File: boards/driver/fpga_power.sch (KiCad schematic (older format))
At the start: 30 parts, among them J1 Barrel_Jack, Q90 IRF530, U10 74LVC245, U11 JTE0624D05, U12 LTC4231-1, U13 74HC4514, U14 74LVC2G04, U15 74LVC2G04, U16 74LVC2G04, U17 74LVC2G04, U9 74LVC245

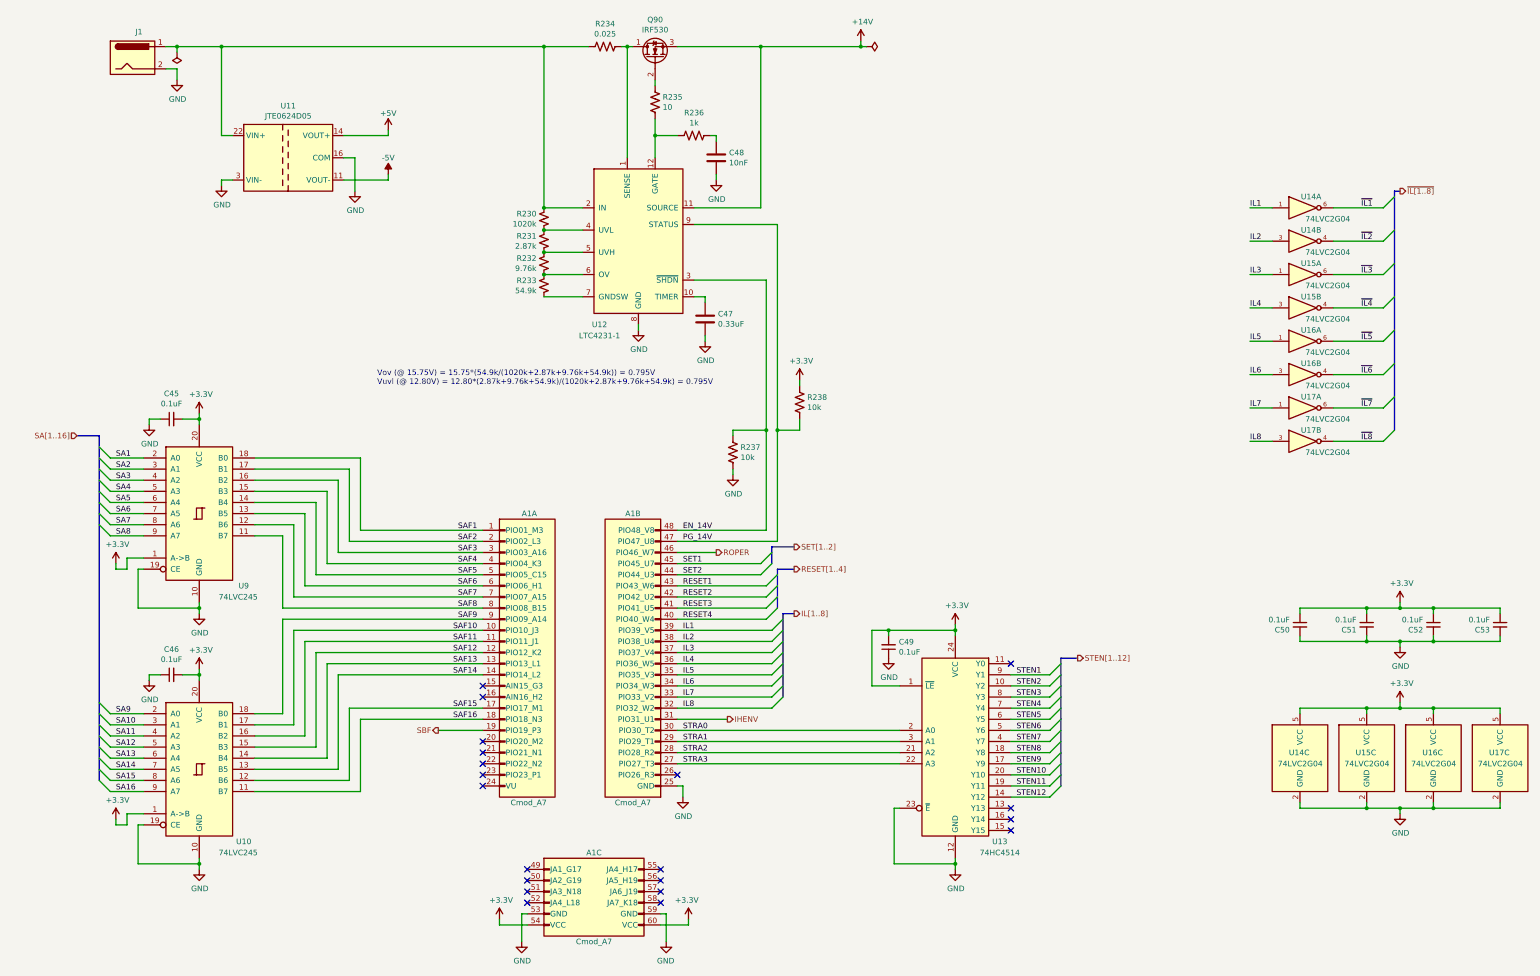
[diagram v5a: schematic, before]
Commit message: Driver board: significant cleanup. Moved sense amp pairs into a subsheet, split tuning resistors into two globally, pushed input circuits into their corresponding sheets.
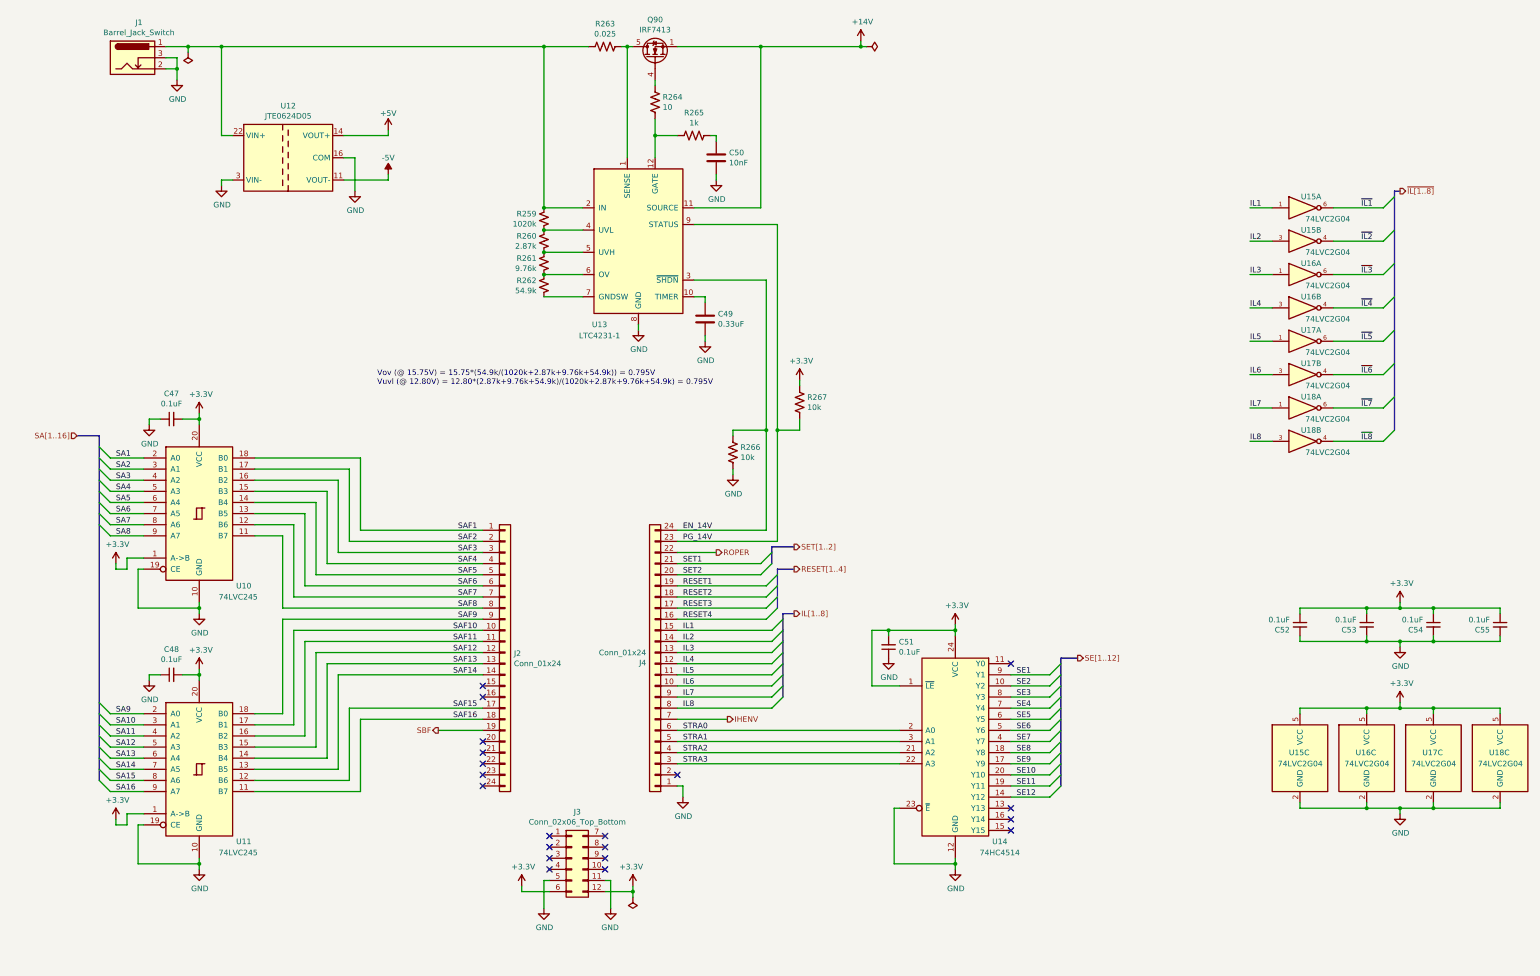
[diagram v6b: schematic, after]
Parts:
- removed A1: Cmod_A7, symbol lachesis:Cmod_A7
- removed J1: Barrel_Jack, symbol Connector:Barrel_Jack
- removed Q90: IRF530, symbol Device:Q_NMOS_DGS
- added J1: Barrel_Jack_Switch, Connector_BarrelJack:BarrelJack_Horizontal, symbol Connector:Barrel_Jack_Switch
- added J2, J4: Conn_01x24, Connector_PinSocket_2.54mm:PinSocket_1x24_P2.54mm_Vertical, symbol Connector_Generic:Conn_01x24
- added J3: Conn_02x06_Top_Bottom, Connector_PinSocket_2.54mm:PinSocket_2x06_P2.54mm_Vertical, symbol Connector_Generic:Conn_02x06_Top_Bottom
- added Q90: IRF7413, Package_SO:SO-8_3.9x4.9mm_P1.27mm, symbol lachesis:Q_NMOS_SO8
- C47: renamed from C45; footprint (none) -> Capacitor_SMD:C_0603_1608Metric
- C48: renamed from C46; footprint (none) -> Capacitor_SMD:C_0603_1608Metric
- C49: renamed from C47; footprint (none) -> Capacitor_SMD:C_0603_1608Metric
- C50: renamed from C48; footprint (none) -> Capacitor_SMD:C_0603_1608Metric
- C51: renamed from C49; footprint (none) -> Capacitor_SMD:C_0603_1608Metric
- C52: renamed from C50; footprint (none) -> Capacitor_SMD:C_0603_1608Metric
- C53: renamed from C51; footprint (none) -> Capacitor_SMD:C_0603_1608Metric
- C54: renamed from C52; footprint (none) -> Capacitor_SMD:C_0603_1608Metric
- C55: renamed from C53; footprint (none) -> Capacitor_SMD:C_0603_1608Metric
- R259: renamed from R230; footprint (none) -> Resistor_SMD:R_0603_1608Metric
- R260: renamed from R231; footprint (none) -> Resistor_SMD:R_0603_1608Metric
- R261: renamed from R232; footprint (none) -> Resistor_SMD:R_0603_1608Metric
- R262: renamed from R233; footprint (none) -> Resistor_SMD:R_0603_1608Metric
- R263: renamed from R234; footprint (none) -> Resistor_SMD:R_0603_1608Metric
- R264: renamed from R235; footprint (none) -> Resistor_SMD:R_0603_1608Metric
- R265: renamed from R236; footprint (none) -> Resistor_SMD:R_0603_1608Metric
- R266: renamed from R237; footprint (none) -> Resistor_SMD:R_0603_1608Metric
- R267: renamed from R238; footprint (none) -> Resistor_SMD:R_0603_1608Metric
- U13: renamed from U12; footprint (none) -> Package_SO:MSOP-12_3x4mm_P0.65mm
- renumbered U9 to U10, U10 to U11, U11 to U12, U13 to U14, U14 to U15, U15 to U16, U16 to U17, U17 to U18
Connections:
- net +14V: now also Q90.1 (S), Q90.2 (S), Q90.3 (S)
- net +3V3: now also J3.12 (Pin_12), J3.6 (Pin_6)
- net EN_14V: now also J4.24 (Pin_24)
- net GND: now also J1.2, J1.3, J3.11 (Pin_11), J3.5 (Pin_5), J4.1 (Pin_1)
- net IHENV: now also J4.7 (Pin_7)
- net IL1: now also J4.15 (Pin_15)
- net IL2: now also J4.14 (Pin_14)
- net IL3: now also J4.13 (Pin_13)
- net IL4: now also J4.12 (Pin_12)
- net IL5: now also J4.11 (Pin_11)
- net IL6: now also J4.10 (Pin_10)
- net IL7: now also J4.9 (Pin_9)
- net IL8: now also J4.8 (Pin_8)
- net PG_14V: now also J4.23 (Pin_23)
- net RESET1: now also J4.19 (Pin_19)
- net RESET2: now also J4.18 (Pin_18)
- net RESET3: now also J4.17 (Pin_17)
- net RESET4: now also J4.16 (Pin_16)
- net ROPER: now also J4.22 (Pin_22)
- net SAF1: now also J2.1 (Pin_1)
- net SAF10: now also J2.10 (Pin_10)
- net SAF11: now also J2.11 (Pin_11)
- net SAF12: now also J2.12 (Pin_12)
- net SAF13: now also J2.13 (Pin_13)
- net SAF14: now also J2.14 (Pin_14)
- net SAF15: now also J2.17 (Pin_17)
- net SAF16: now also J2.18 (Pin_18)
- net SAF2: now also J2.2 (Pin_2)
- net SAF3: now also J2.3 (Pin_3)
- net SAF4: now also J2.4 (Pin_4)
- net SAF5: now also J2.5 (Pin_5)
- net SAF6: now also J2.6 (Pin_6)
- net SAF7: now also J2.7 (Pin_7)
- net SAF8: now also J2.8 (Pin_8)
- net SAF9: now also J2.9 (Pin_9)
- net SBF: now also J2.19 (Pin_19)
- net SET1: now also J4.21 (Pin_21)
- net SET2: now also J4.20 (Pin_20)
- net STRA0: now also J4.6 (Pin_6)
- net STRA1: now also J4.5 (Pin_5)
- net STRA2: now also J4.4 (Pin_4)
- net STRA3: now also J4.3 (Pin_3)
- net at R259.2, R263.2, U12.22 (VIN+)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: now also J1.1
- net at R263.1, U13.1 (SENSE): now also Q90.5 (D), Q90.6 (D), Q90.7 (D), Q90.8 (D)
- net at R264.1: now also Q90.4 (G)
- net STEN1 renamed SE1
- net STEN10 renamed SE10
- net STEN11 renamed SE11
- net STEN12 renamed SE12
- net STEN2 renamed SE2
- net STEN3 renamed SE3
- net STEN4 renamed SE4
- net STEN5 renamed SE5
- net STEN6 renamed SE6
- net STEN7 renamed SE7
- net STEN8 renamed SE8
- net STEN9 renamed SE9

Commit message: Driver: incorporated some power LEDs
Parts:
- added D160: BLUE, symbol Device:LED_ALT
- added D161: TEAL, symbol Device:LED_ALT
- added D162: ORANGE, symbol Device:LED_ALT
- added R268, R269: 430, Resistor_SMD:R_0603_1608Metric, symbol Device:R_US
- added R270: 12k, symbol Device:R_US
- added R271: 2.4k, symbol Device:R_US
- added R272: 620, Resistor_SMD:R_0603_1608Metric, symbol Device:R_US
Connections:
- net +14V: now also R272.1
- net +5V: now also R269.1, R271.2
- net -5V: now also R268.1
- net GND: now also D160.2 (A), D161.1 (K), D162.1 (K)
- net at J1.1, R259.2, R263.2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: now also R270.2
- net ADC_14V: now reaches J2.15 (Pin_15)
- net ADC_14V: now also R270.1
- net ADC_5V: now reaches J2.16 (Pin_16)
- net ADC_5V: now also R271.1
- new net: D162.2 (A), R272.2
- new net: D161.2 (A), R269.2
- new net: D160.1 (K), R268.2
- no-connect marks 20 -> 18
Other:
- moved on the sheet: J1, U12
